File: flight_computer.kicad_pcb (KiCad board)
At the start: 4 copper layers, 95.9 x 90.2 mm, 157 parts, among them J1 436500204, J10 TSW-102-07-F-S, J11 TSW-103-07-F-S, J12 SMA-J-P-H-ST-EM1, J2 0530480210, J3 0530480210, J4 398800302, J5 398800302, J6 398800302, J7 398800302, J8 0530480810, J9 USB4105-GF-A-120, Q6 SI1016CX-T1-GE3, Q7 DMT6007LFGQ-7, U1 STM32F405VGT7, U10 LT6000IDCB#TRMPBF, U11 NC7WZ07P6X, U12 B39162B4300F210, U13 MS561101BA03-50, U14 IAM-20380HT, U15 H3LIS331DLTR, U16 LM74700QDRQ1, U2 INA229AQDGSRQ1, U3 TPS62130AQRGTRQ1, U4 TPS62130AQRGTRQ1, U5 S25FL256LAGNFM010, U6 USBLC6-2P6, U7 MMC5983MA, U8 AIS2IHTR, U9 MAX-M10S-00B, Y1 25MHz

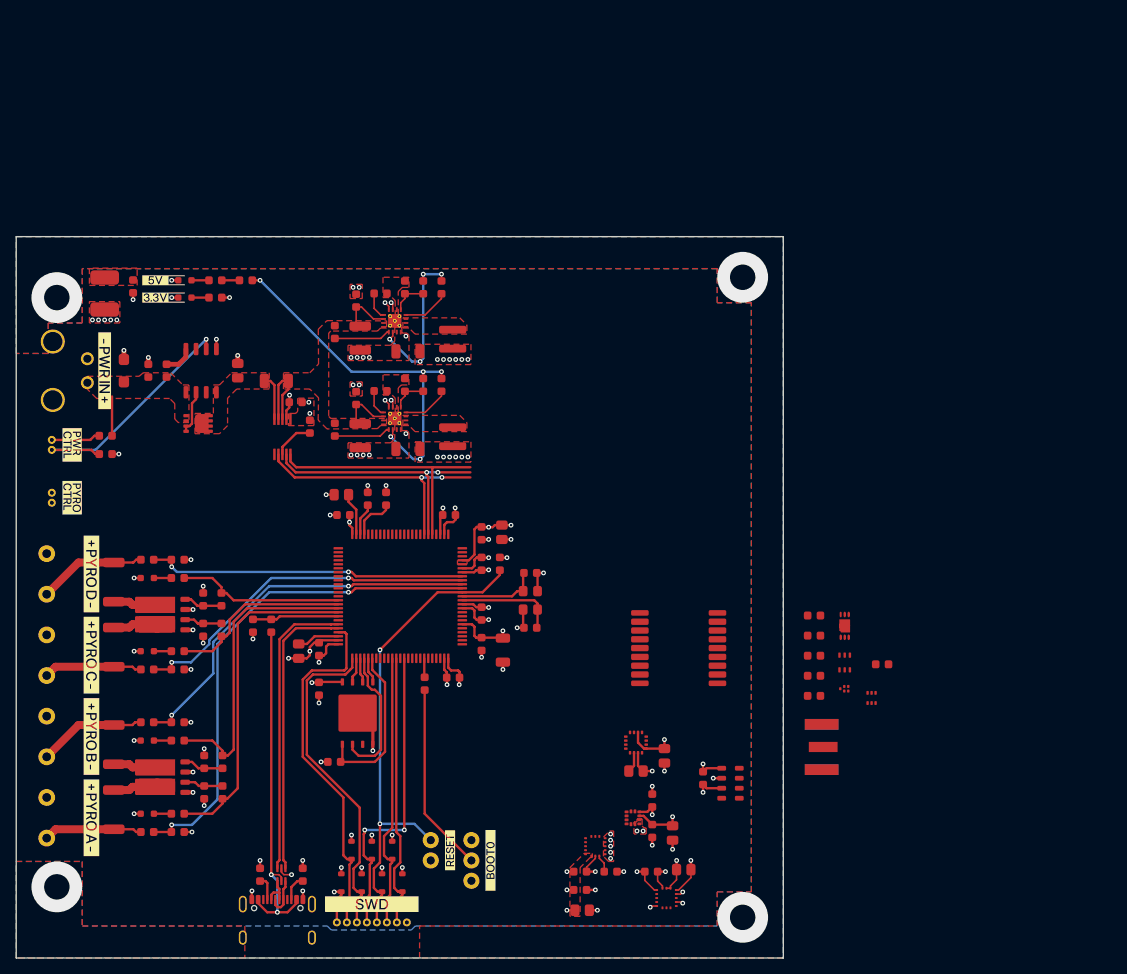
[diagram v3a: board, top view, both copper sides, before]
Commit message: Add initial layout for the GNSS receiver
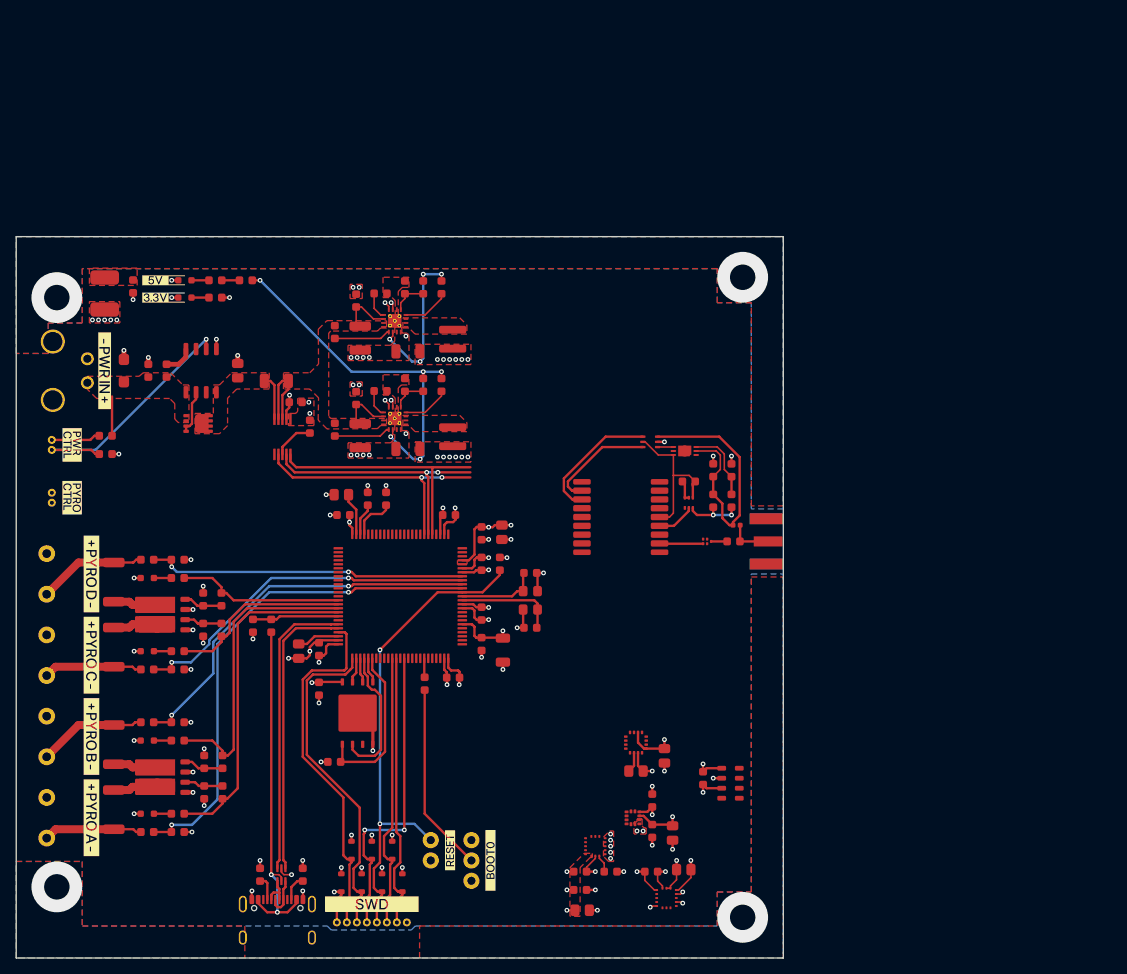
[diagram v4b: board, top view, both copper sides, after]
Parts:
- added L3: 27nH, passive_inductor:L_0402_Density_Nominal, F.Cu at (194.7, 86.6)
- U1: value STM32F405VGT7 -> LQFP100
- U6: value USBLC6-2P6 -> SOT-666-6
- moved U11 36.8 mm to (183.9, 76.2), turned to 90 degrees
- moved Q6 33.4 mm to (188.8, 83.8)
- moved U10 29.6 mm to (188.3, 77.3), turned to 90 degrees
- moved R52 27.7 mm to (194.1, 79.7), turned to 90 degrees
- moved R51 26.8 mm to (188.8, 81.1)
- moved J12 26.6 mm to (200.6, 88.6)
- moved R53 26.5 mm to (194.1, 83.5), turned to 90 degrees
- moved U12 25.2 mm to (191.1, 88.6), turned to 180 degrees
- moved C33 24.1 mm to (194.4, 88.6)
- moved C32 22.1 mm to (191.8, 79.7), turned to 90 degrees
- moved R50 21.0 mm to (191.8, 83.5), turned to -90 degrees
- moved U9 17.9 mm to (180.3, 85.6), turned to 180 degrees
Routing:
- net Net-(U10-IN-): track 0.00 -> 33.8 mm
- net VCC RF: track 0.00 -> 19.2 mm
- net /rf/ANT_SHORT: track 0.00 -> 16.3 mm
- net /rf/ANT_DETECT: track 0.00 -> 13.7 mm
- net Net-(U10-IN+): track 0.00 -> 9.31 mm
- net Net-(Q6B-D): track 0.00 -> 7.37 mm, vias 0 -> 2
- net Net-(C33-Pad2): track 0.00 -> 5.68 mm
- net /rf/RF_IN: track 0.00 -> 5.46 mm
- net /rf/LNA_EN: track 0.00 -> 4.81 mm
- net GND: track 114.5 -> 117.3 mm, vias 101 -> 104
- net Net-(Q6A-D): track 0.00 -> 2.65 mm
- net Net-(U12-Input): track 0.00 -> 2.00 mm
- net Net-(U10-OUT): track 0.00 -> 1.98 mm
- added copper zone on B.Cu, net (none)

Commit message: Improve board grounding for RF
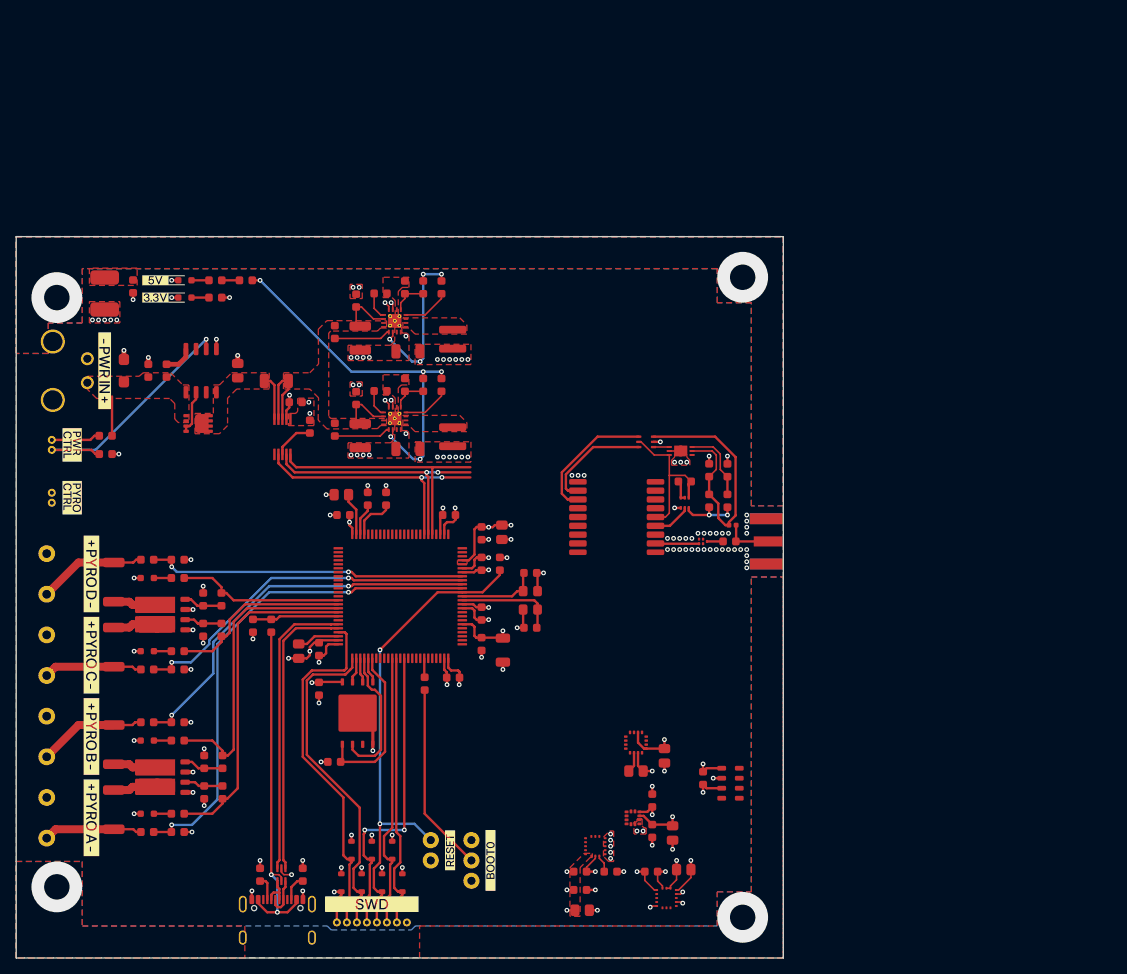
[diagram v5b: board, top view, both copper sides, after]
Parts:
- moved C32 0.51 mm to (191.3, 79.7)
- moved C33 0.51 mm to (193.9, 88.6)
- moved L3 0.51 mm to (194.2, 86.6)
- moved Q6 0.51 mm to (188.3, 83.8)
- moved R50 0.51 mm to (191.3, 83.5)
- moved R51 0.51 mm to (188.3, 81.1)
- moved R52 0.51 mm to (193.6, 79.7)
- moved R53 0.51 mm to (193.6, 83.5)
- moved U10 0.51 mm to (187.8, 77.3)
- moved U11 0.51 mm to (183.4, 76.2)
- moved U12 0.51 mm to (190.6, 88.6)
- moved U9 0.51 mm to (179.8, 85.6)
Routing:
- net GND: track 117.3 -> 119.5 mm, vias 104 -> 143
- net Net-(C33-Pad2): track 5.68 -> 6.18 mm
- added copper zone on B.Cu, net GND
- removed copper zone on B.Cu, net (none)
